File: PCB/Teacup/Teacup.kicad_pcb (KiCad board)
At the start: 4 copper layers, 86.2 x 56.2 mm, 93 parts, among them IC1 T31ZX, J1 USB Type-C, J2 SD_Card, J3 SFW15R-2STE1LF, J4 EXP0, J5 UART, J6 EXP2, J7 EXP1, U1 AZ1117-3.3, U2 AZ1117-1.8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

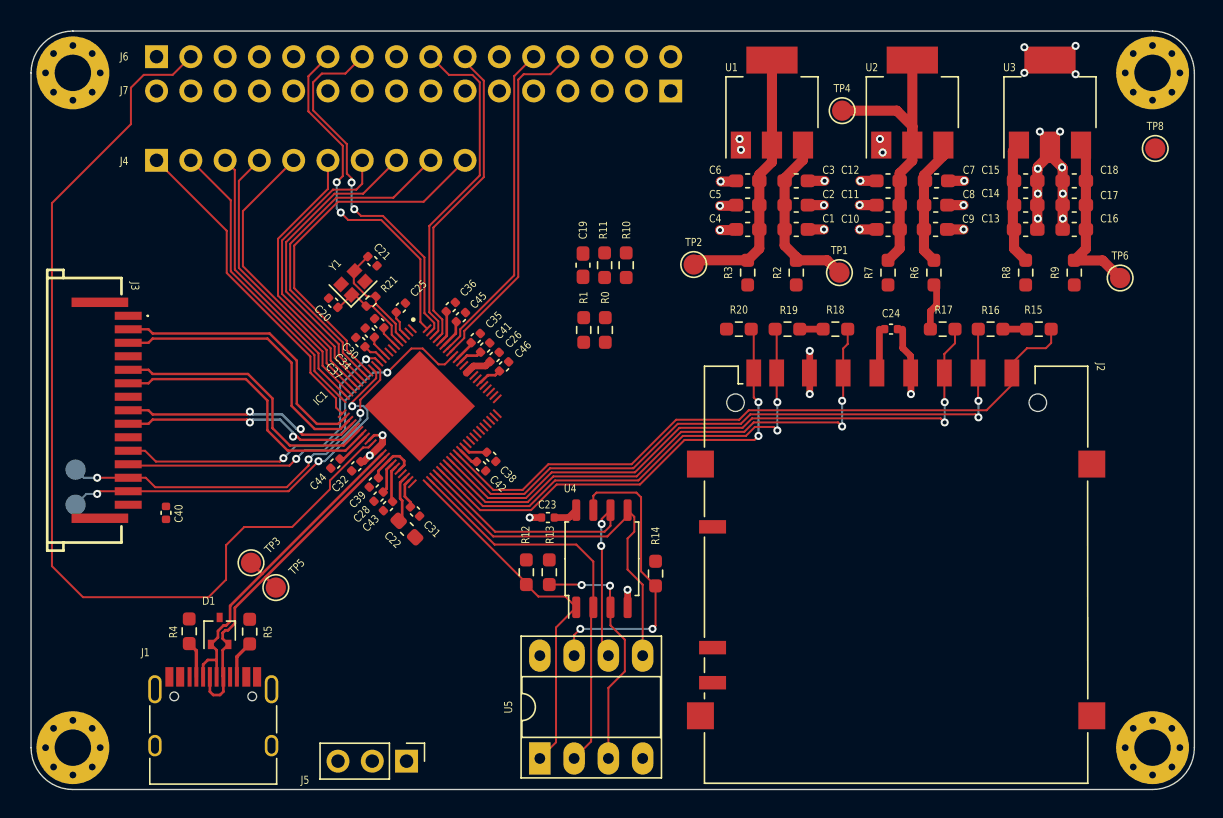
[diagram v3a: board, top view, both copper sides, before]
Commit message: pcb: routing done
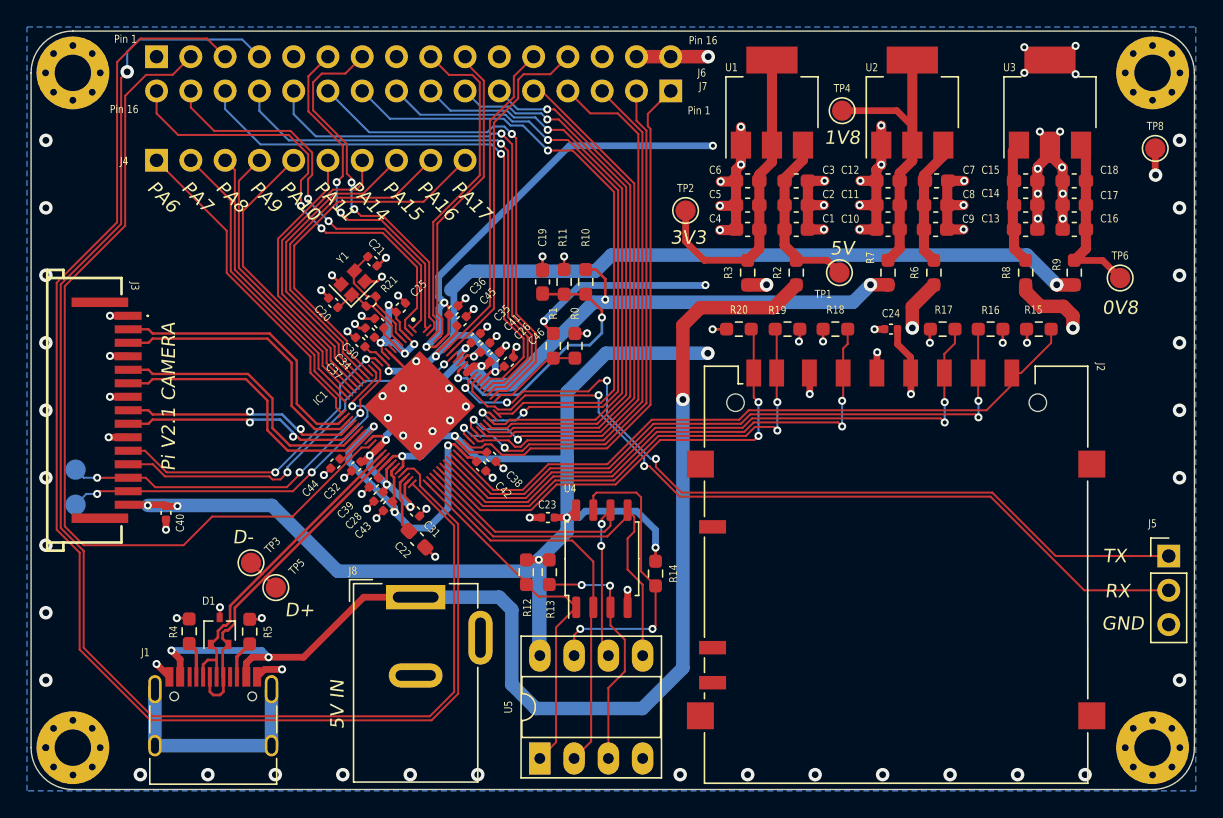
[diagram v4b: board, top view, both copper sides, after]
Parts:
- added G***: LOGO, LOGO, B.Cu at (226.0, 82.2)
- added J8: DC_IN, Connector_BarrelJack:BarrelJack_Wuerth_6941xx301002, F.Cu at (190.4, 93.8)
- moved J5 58.5 mm to (246.2, 90.8), turned to 0 degrees
- moved TP2 4.04 mm to (210.4, 65.2)
- moved C19 3.25 mm to (199.8, 70.5)
- moved R10 3.25 mm to (203.0, 70.5)
- moved R11 3.25 mm to (201.4, 70.5)
- moved R0 2.54 mm to (202.2, 75.2)
- moved R1 2.54 mm to (200.6, 75.2)
- moved C22 1.06 mm to (190.5, 89.5)
- moved C46 0.49 mm to (197.3, 76.4)
- moved C36 0.32 mm to (193.2, 72.6)
- moved C45 0.30 mm to (193.8, 73.4)
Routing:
- net +3V3: track 20.6 -> 181.9 mm, vias 0 -> 25
- net /MICLP: track 0.00 -> 105.5 mm
- net /HPOUTL: track 0.00 -> 104.6 mm, vias 0 -> 1
- net +0V8: track 14.3 -> 112.6 mm, vias 0 -> 8
- net +5V: track 0.00 -> 88.0 mm, vias 0 -> 3
- net +1V8: track 18.3 -> 86.3 mm, vias 2 -> 12
- net GND: track 37.5 -> 103.2 mm, vias 33 -> 109
- net /UART_TX: track 0.00 -> 61.7 mm, vias 0 -> 4
- net /UART_RX: track 0.00 -> 60.8 mm, vias 0 -> 2
- net Net-(IC1-Pad65): track 0.00 -> 46.5 mm, vias 0 -> 3
- net Net-(IC1-Pad66): track 0.00 -> 45.8 mm, vias 0 -> 1
- net Net-(IC1-Pad64): track 0.00 -> 43.2 mm, vias 0 -> 1
- net Net-(IC1-Pad71): track 0.00 -> 42.7 mm, vias 0 -> 1
- net Net-(IC1-Pad63): track 0.00 -> 41.8 mm, vias 0 -> 1
- net Net-(IC1-Pad60): track 0.00 -> 41.6 mm, vias 0 -> 2
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- added copper zone on In2.Cu, net +0V8
- added copper zone on In2.Cu, net +1V8
- added copper zone on In2.Cu, net +3V3
- added copper zone on B.Cu, net GND
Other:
- board text added: "${TITLE} Rev.${REVISION} - ${COMPANY} (c) 2023"
- board text added: "0V8"
- board text added: "1V8"
- board text added: "3V3"
- board text added: "5V"
- board text added: "5V IN"
- board text added: "D+"
- board text added: "D-"
- board text added: "EXP0"
- board text added: "EXP1"
- board text added: "EXP2"
- board text added: "GND"
- board text added: "PA10"
- board text added: "PA11"
- board text added: "PA14"
- board text added: "PA15"
- board text added: "PA16"
- board text added: "PA17"
- board text added: "PA6"
- board text added: "PA7"
- board text added: "PA8"
- board text added: "PA9"
- board text added: "Pi V2.1 CAMERA"
- board text added: "Pin 1"
- board text added: "Pin 16"
- board text added: "RX"
- board text added: "SCL"
- board text added: "SDA"
- board text added: "TX"

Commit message: pcb: boms and gerbers
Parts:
- C1, C10, C13, C16, C4, C7: footprint Capacitor_SMD:C_0603_1608Metric_Pad1.08x0.95mm_HandSolder -> Capacitor_SMD:C_0805_2012Metric_Pad1.18x1.45mm_HandSolder
- C20, C21: value TBD -> 12pF
- moved C7 3.61 mm to (229.2, 66.6)
- moved C9 3.60 mm to (228.9, 63.0)
- moved C1 0.20 mm to (218.8, 66.6)
- moved C10 0.20 mm to (225.2, 66.6)
- moved C16 0.20 mm to (239.4, 66.6)
- moved C13 0.20 mm to (235.4, 66.6)
- moved C4 0.20 mm to (214.8, 66.6)
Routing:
- net GND: track 103.2 -> 104.0 mm
